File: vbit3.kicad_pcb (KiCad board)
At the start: 2 copper layers, 65 x 56 mm, 49 parts, among them Q1 DTC143E, U1 SAA7113, U3 SAA7120H, U4 74LVC157, U5 23K256, X1 24.576MHz

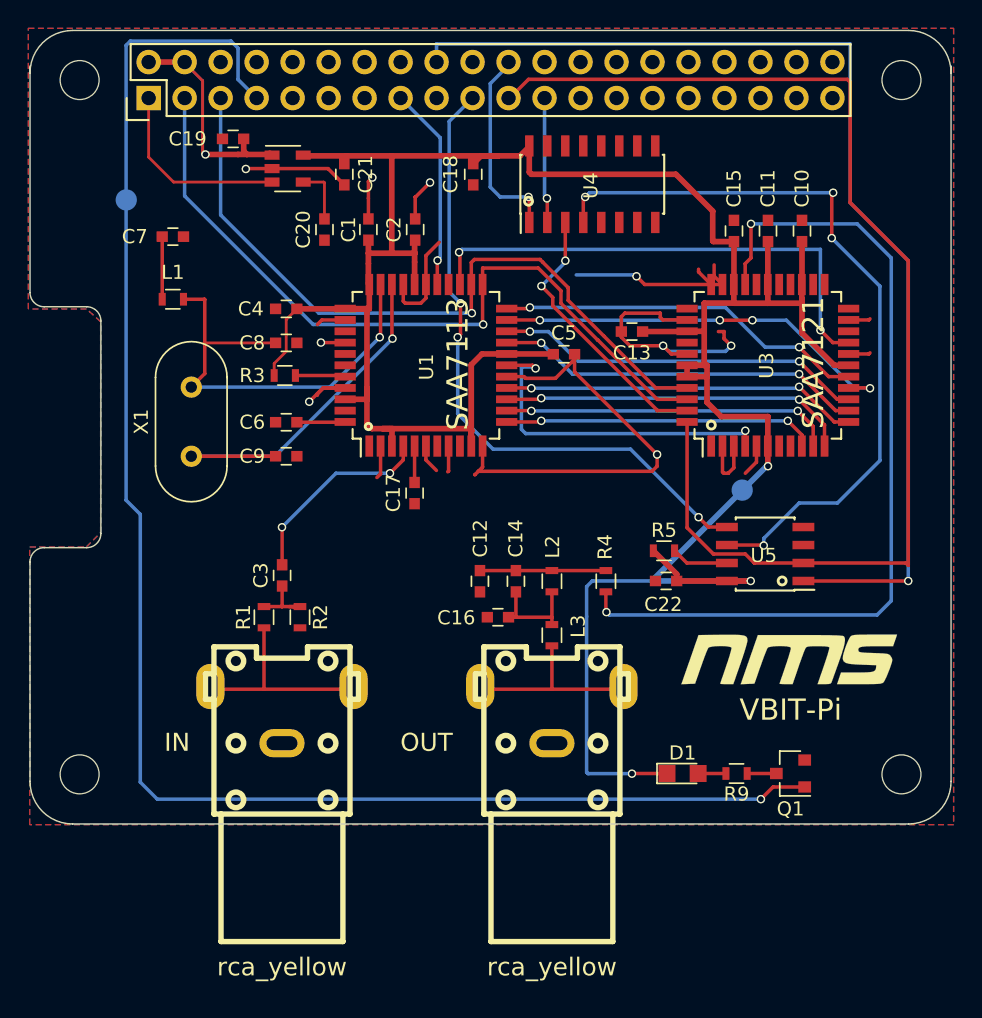
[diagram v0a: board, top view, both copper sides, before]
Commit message: Made some design for manufacturability layout improvements, changed some footprints and updated BOM
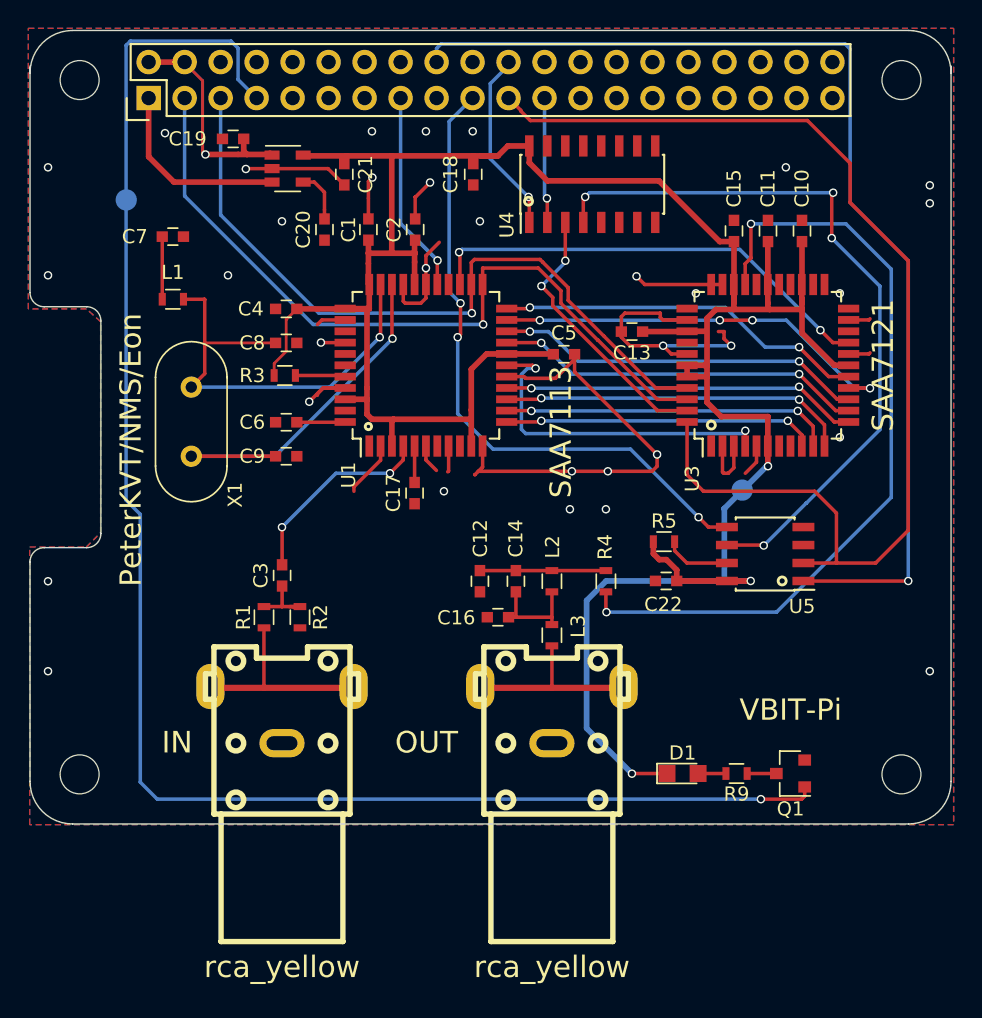
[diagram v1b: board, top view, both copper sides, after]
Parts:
- removed the ? at (162.8, 114.7)
- moved R5 0.64 mm to (154.0, 106.4)
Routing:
- net +3.3V: track 232.2 -> 205.7 mm
- net Net-(L3-Pad2): track 13.3 -> 23.4 mm
- net Net-(P2-Pad1): track 14.6 -> 24.7 mm
- net GND: track 108.9 -> 103.0 mm, vias 9 -> 32
- net Net-(R4-Pad1): track 61.6 -> 56.7 mm
- net MISO: track 84.7 -> 80.9 mm
- net /RTC: track 35.9 -> 32.6 mm
- net FLD: track 14.4 -> 17.1 mm
- net Net-(U4-Pad4): track 53.4 -> 51.9 mm
- net MUX: track 14.2 -> 13.0 mm
- net Net-(R5-Pad2): track 4.14 -> 4.78 mm
- net (no net): vias 0 -> 1
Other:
- board text added: "PeterKVT/NMS/Eon"
- board text added: "Version 3.2"
- board text removed: "Version 3.1"
